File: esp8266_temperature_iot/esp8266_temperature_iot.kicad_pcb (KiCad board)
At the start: 2 copper layers, 51.7 x 149.8 mm, 26 parts, among them J1 Screw_Terminal_01x09, J2 Screw_Terminal_01x09, U1 WeMos_D1_mini, U2 MCP3208

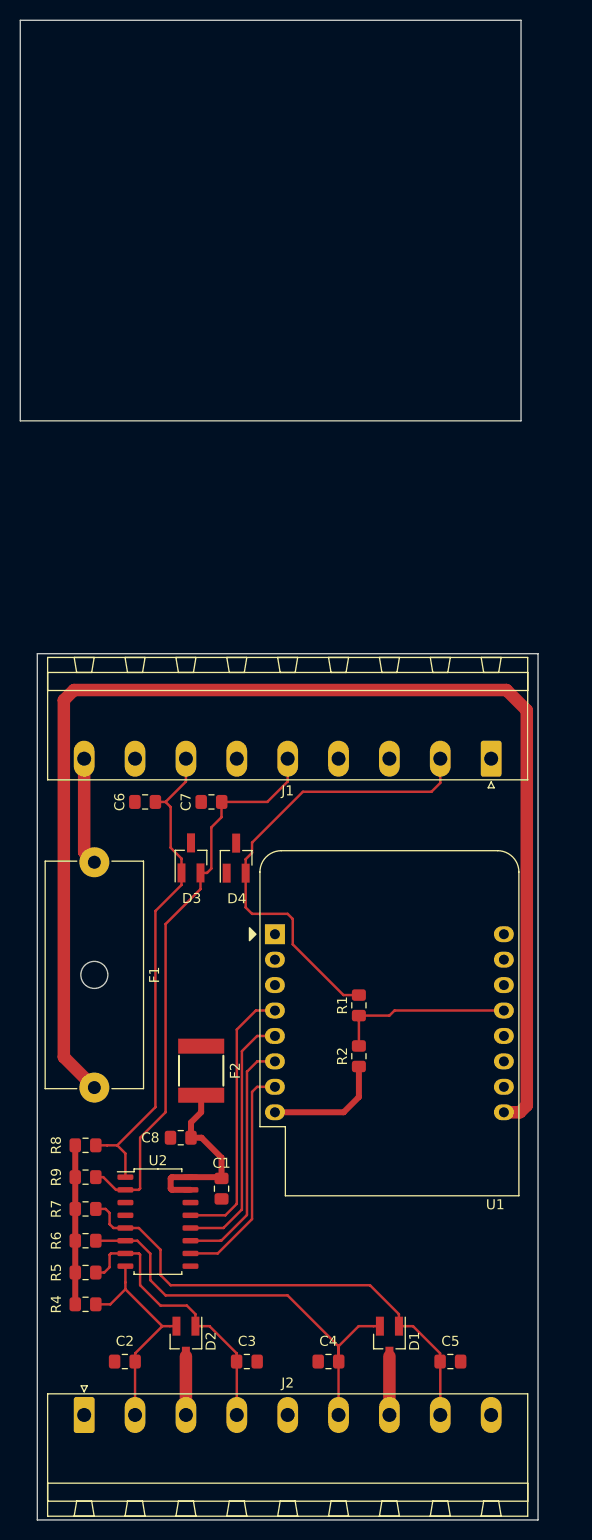
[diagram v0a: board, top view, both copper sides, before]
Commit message: Nicer looking PCB (thicker wires + ground pour)
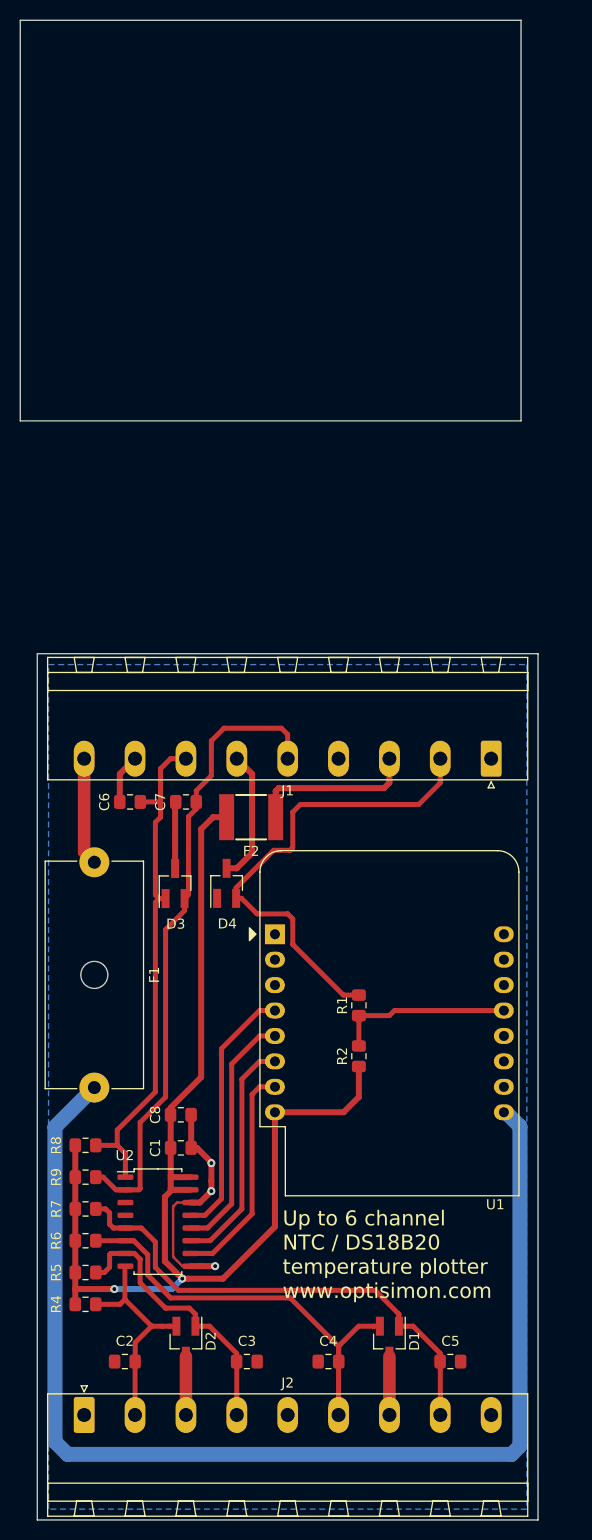
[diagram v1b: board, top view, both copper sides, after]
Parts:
- moved F2 25.8 mm to (72.6, 100.1), turned to 180 degrees
- moved C1 5.75 mm to (65.5, 133.1), turned to 0 degrees
- moved D3 3.02 mm to (65.0, 106.7)
- moved D4 2.69 mm to (70.1, 106.7)
- moved C7 2.54 mm to (66.0, 98.6)
- moved C8 2.29 mm to (65.5, 129.8), turned to 0 degrees
- moved C6 1.51 mm to (60.5, 98.6)
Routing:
- net +3V3: track 46.8 -> 116.0 mm, vias 0 -> 2
- net Earth: track 11.7 -> 59.4 mm, vias 0 -> 3
- net OneWire_+: track 0.00 -> 16.7 mm
- net +5V: track 129.5 -> 118.4 mm
- net NTC5: track 57.1 -> 63.5 mm
- net NTC4: track 49.4 -> 51.0 mm
- net SCLK: track 27.1 -> 25.7 mm
- net OneWire_DQ_EXT: track 46.8 -> 48.0 mm
- net MISO: track 25.6 -> 24.6 mm
- net MOSI: track 24.2 -> 23.4 mm
- added copper zone on B.Cu, net Earth
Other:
- board text added: "Up to 6 channel NTC / DS18B20 temperature plotter www.optisimon.com"

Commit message: Even nicer - everything double checked. Ready for order
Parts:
- added J3: Conn_01x04_Male, Connector_PinHeader_2.54mm:PinHeader_1x04_P2.54mm_Vertical, F.Cu at (67.6, 113.3)
- added R3: 1k, Resistor_SMD:R_1210_3225Metric_Pad1.42x2.65mm_HandSolder, F.Cu at (66.0, 125.5)
- moved R1 0.92 mm to (82.5, 119.4), turned to 180 degrees
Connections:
- U1 pad 1: (no net) -> Net-(J3-Pad1)
- U1 pad 14: (no net) -> LED1
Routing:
- net LED1: track 0.00 -> 52.5 mm
- net Earth: track 59.4 -> 87.7 mm, vias 3 -> 5
- net Net-(J3-Pad1): track 0.00 -> 8.00 mm
- net Net-(J3-Pad4): track 0.00 -> 4.60 mm
- net OneWire_DQ_EXT: track 48.0 -> 50.3 mm
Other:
- board size 51.7 x 149.8 mm -> 50 x 86.5 mm
- board text added: "GND"
- board text added: "GND +5V NTC0 GND GND NTC4 NTC1 GND GND NTC5 NTC2 GND GND OW_+ NTC3 OW_DQ GND GND"
- board text added: "L+"
- board text added: "L-"
- board text added: "RST"
